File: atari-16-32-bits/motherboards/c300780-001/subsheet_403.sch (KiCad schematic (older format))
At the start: 43 parts, among them Q404 2N3904, Q405 2N3904, U403 MC1377_COLOR_TELEVISION_RGB_T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

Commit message: [PCB] Assign builtins footprint when possible - resistors, ports
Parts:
- D401, D402: footprint (none) -> Diode_THT:D_DO-35_SOD27_P7.62mm_Horizontal
- DL1: footprint (none) -> Delay_Line_Custom_Atari_ST:Delay_Line_Custom_Atari_ST
- MOD1: footprint (none) -> Connector_PinHeader_2.54mm:PinHeader_1x03_P2.54mm_Vertical
- R405, R439, R448, R451, R452, R456, R459, R463, R467, R468, R469, R470, R471, R473, R474, R475: footprint (none) -> Resistor_THT:R_Axial_DIN0204_L3.6mm_D1.6mm_P7.62mm_Horizontal
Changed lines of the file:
@@
 F 0 "R471" V 2300 4650 50  0000 C CNN
 F 1 "47K" V 2500 4650 50  0000 C CNN
-F 2 "" H 2400 4650 50  0001 C CNN
+F 2 "Resistor_THT:R_Axial_DIN0204_L3.6mm_D1.6mm_P7.62mm_Horizontal" H 2400 4650 50  0001 C CNN
 F 3 "~" H 2400 4650 50  0001 C CNN
 	1    2400 4650
@@
 F 0 "R470" H 4680 5920 50  0000 L CNN
 F 1 "1K" H 4680 5860 50  0000 L CNN
-F 2 "" H 4650 5900 50  0001 C CNN
+F 2 "Resistor_THT:R_Axial_DIN0204_L3.6mm_D1.6mm_P7.62mm_Horizontal" H 4650 5900 50  0001 C CNN
 F 3 "~" H 4650 5900 50  0001 C CNN
 	1    4650 5900
@@
 F 0 "R469" V 4300 5650 50  0000 C CNN
 F 1 "5K6" V 4500 5650 50  0000 C CNN
-F 2 "" H 4400 5650 50  0001 C CNN
+F 2 "Resistor_THT:R_Axial_DIN0204_L3.6mm_D1.6mm_P7.62mm_Horizontal" H 4400 5650 50  0001 C CNN
 F 3 "~" H 4400 5650 50  0001 C CNN
 	1    4400 5650
@@
 F 0 "R459" H 7180 5020 50  0000 L CNN
 F 1 "0" H 7180 4960 50  0000 L CNN
-F 2 "" H 7150 5000 50  0001 C CNN
+F 2 "Resistor_THT:R_Axial_DIN0204_L3.6mm_D1.6mm_P7.62mm_Horizontal" H 7150 5000 50  0001 C CNN
 F 3 "~" H 7150 5000 50  0001 C CNN
 	1    7150 5000
@@
 F 0 "R405" V 3850 5950 50  0000 C CNN
 F 1 "0" V 4050 5950 50  0000 C CNN
-F 2 "" H 3950 5950 50  0001 C CNN
+F 2 "Resistor_THT:R_Axial_DIN0204_L3.6mm_D1.6mm_P7.62mm_Horizontal" H 3950 5950 50  0001 C CNN
 F 3 "~" H 3950 5950 50  0001 C CNN
 	1    3950 5950
@@
 F 0 "R439" H 5930 6320 50  0000 L CNN
 F 1 "75" H 5930 6260 50  0000 L CNN
-F 2 "" H 5900 6300 50  0001 C CNN
+F 2 "Resistor_THT:R_Axial_DIN0204_L3.6mm_D1.6mm_P7.62mm_Horizontal" H 5900 6300 50  0001 C CNN
 F 3 "~" H 5900 6300 50  0001 C CNN
 	1    5900 6300
@@
 F 0 "R452" H 5930 7820 50  0000 L CNN
 F 1 "1K5" H 5930 7760 50  0000 L CNN
-F 2 "" H 5900 7800 50  0001 C CNN
+F 2 "Resistor_THT:R_Axial_DIN0204_L3.6mm_D1.6mm_P7.62mm_Horizontal" H 5900 7800 50  0001 C CNN
 F 3 "~" H 5900 7800 50  0001 C CNN
 	1    5900 7800
@@
 F 0 "R456" H 5930 8320 50  0000 L CNN
 F 1 "2K2" H 5930 8260 50  0000 L CNN
-F 2 "" H 5900 8300 50  0001 C CNN
+F 2 "Resistor_THT:R_Axial_DIN0204_L3.6mm_D1.6mm_P7.62mm_Horizontal" H 5900 8300 50  0001 C CNN
 F 3 "~" H 5900 8300 50  0001 C CNN
 	1    5900 8300
@@
 F 0 "DL1" H 2050 6650 50  0000 L CNN
 F 1 "Delay Line 3.58MHz" H 2050 6050 50  0000 L CNN
-F 2 "" H 2000 6350 50  0001 C CNN
+F 2 "Delay_Line_Custom_Atari_ST:Delay_Line_Custom_Atari_ST" H 2000 6350 50  0001 C CNN
 F 3 "~" H 2000 6350 50  0001 C CNN
 	1    2000 6350
@@
 F 0 "R467" H 2030 5770 50  0000 L CNN
 F 1 "1K2" H 2030 5710 50  0000 L CNN
-F 2 "" H 2000 5750 50  0001 C CNN
+F 2 "Resistor_THT:R_Axial_DIN0204_L3.6mm_D1.6mm_P7.62mm_Horizontal" H 2000 5750 50  0001 C CNN
 F 3 "~" H 2000 5750 50  0001 C CNN
 	1    2000 5750
@@
 F 0 "R468" H 2030 7070 50  0000 L CNN
 F 1 "1K2" H 2030 7010 50  0000 L CNN
-F 2 "" H 2000 7050 50  0001 C CNN
+F 2 "Resistor_THT:R_Axial_DIN0204_L3.6mm_D1.6mm_P7.62mm_Horizontal" H 2000 7050 50  0001 C CNN
 F 3 "~" H 2000 7050 50  0001 C CNN
 	1    2000 7050
@@
 F 0 "R448" H 5430 7320 50  0000 L CNN
 F 1 "150" H 5430 7260 50  0000 L CNN
-F 2 "" H 5400 7300 50  0001 C CNN
+F 2 "Resistor_THT:R_Axial_DIN0204_L3.6mm_D1.6mm_P7.62mm_Horizontal" H 5400 7300 50  0001 C CNN
 F 3 "~" H 5400 7300 50  0001 C CNN
 	1    5400 7300
@@
 F 0 "R463" H 3930 8020 50  0000 L CNN
 F 1 "1K" H 3930 7960 50  0000 L CNN
-F 2 "" H 3900 8000 50  0001 C CNN
+F 2 "Resistor_THT:R_Axial_DIN0204_L3.6mm_D1.6mm_P7.62mm_Horizontal" H 3900 8000 50  0001 C CNN
 F 3 "~" H 3900 8000 50  0001 C CNN
 	1    3900 8000
@@
 F 0 "R451" H 4430 7320 50  0000 L CNN
 F 1 "0" H 4430 7260 50  0000 L CNN
-F 2 "" H 4400 7300 50  0001 C CNN
+F 2 "Resistor_THT:R_Axial_DIN0204_L3.6mm_D1.6mm_P7.62mm_Horizontal" H 4400 7300 50  0001 C CNN
 F 3 "~" H 4400 7300 50  0001 C CNN
 	1    4400 7300
@@
 F 0 "MOD1" H 6810 8240 50  0000 C CNN
 F 1 "ST Modulator" H 6840 7860 50  0000 L CNN
-F 2 "" H 6800 8050 50  0001 C CNN
+F 2 "Connector_PinHeader_2.54mm:PinHeader_1x03_P2.54mm_Vertical" H 6800 8050 50  0001 C CNN
 F 3 "~" H 6800 8050 50  0001 C CNN
 	1    6800 8050
@@
 F 0 "R473" H 5830 1320 50  0000 L CNN
 F 1 "10K" H 5830 1260 50  0000 L CNN
-F 2 "" H 5800 1300 50  0001 C CNN
+F 2 "Resistor_THT:R_Axial_DIN0204_L3.6mm_D1.6mm_P7.62mm_Horizontal" H 5800 1300 50  0001 C CNN
 F 3 "~" H 5800 1300 50  0001 C CNN
 	1    5800 1300
@@
 F 0 "R475" H 6280 2170 50  0000 L CNN
 F 1 "150" H 6280 2110 50  0000 L CNN
-F 2 "" H 6250 2150 50  0001 C CNN
+F 2 "Resistor_THT:R_Axial_DIN0204_L3.6mm_D1.6mm_P7.62mm_Horizontal" H 6250 2150 50  0001 C CNN
 F 3 "~" H 6250 2150 50  0001 C CNN
 	1    6250 2150
@@
 F 0 "R474" V 6400 1900 50  0000 C CNN
 F 1 "100" V 6600 1900 50  0000 C CNN
-F 2 "" H 6500 1900 50  0001 C CNN
+F 2 "Resistor_THT:R_Axial_DIN0204_L3.6mm_D1.6mm_P7.62mm_Horizontal" H 6500 1900 50  0001 C CNN
 F 3 "~" H 6500 1900 50  0001 C CNN
 	1    6500 1900
@@
 F 0 "D401" H 5400 1650 50  0000 C CNN
 F 1 "1N914" H 5400 1450 50  0000 C CNN
-F 2 "" H 5400 1550 50  0001 C CNN
+F 2 "Diode_THT:D_DO-35_SOD27_P7.62mm_Horizontal" H 5400 1550 50  0001 C CNN
 F 3 "~" H 5400 1550 50  0001 C CNN
 	1    5400 1550
@@
 F 0 "D402" H 5400 2050 50  0000 C CNN
 F 1 "1N914" H 5400 1850 50  0000 C CNN
-F 2 "" H 5400 1950 50  0001 C CNN
+F 2 "Diode_THT:D_DO-35_SOD27_P7.62mm_Horizontal" H 5400 1950 50  0001 C CNN
 F 3 "~" H 5400 1950 50  0001 C CNN
 	1    5400 1950

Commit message: [PCB] continuing footprint assignement
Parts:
- L403: footprint (none) -> variable_coil_shielded:Variable_Coil_Shielded_7x7mm_5_6
- Q404, Q405: footprint Package_TO_SOT_THT:TO-92_Inline -> Package_TO_SOT_THT:TO-92_Inline_Wide
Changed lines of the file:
@@
 F 0 "Q404" H 5500 6700 50  0000 L CNN
 F 1 "2N3904" H 5450 6600 50  0000 L CNN
-F 2 "Package_TO_SOT_THT:TO-92_Inline" H 5500 6625 50  0001 L CIN
+F 2 "Package_TO_SOT_THT:TO-92_Inline_Wide" H 5500 6625 50  0001 L CIN
 F 3 "https://www.onsemi.com/pub/Collateral/2N3903-D.PDF" H 5300 6700 50  0001 L CNN
 	1    5300 6700
@@
 F 0 "Q405" H 6350 1550 50  0000 L CNN
 F 1 "2N3904" H 6300 1450 50  0000 L CNN
-F 2 "Package_TO_SOT_THT:TO-92_Inline" H 6350 1475 50  0001 L CIN
+F 2 "Package_TO_SOT_THT:TO-92_Inline_Wide" H 6350 1475 50  0001 L CIN
 F 3 "https://www.onsemi.com/pub/Collateral/2N3903-D.PDF" H 6150 1550 50  0001 L CNN
 	1    6150 1550
@@
 F 0 "L403" H 4900 7825 50  0000 C CNN
 F 1 "Variable Coil 24uH" H 4900 7450 50  0000 C CNN
-F 2 "" H 4900 7650 50  0001 C CNN
+F 2 "variable_coil_shielded:Variable_Coil_Shielded_7x7mm_5_6" H 4900 7650 50  0001 C CNN
 F 3 "~" H 4900 7650 50  0001 C CNN
 	1    4900 7650

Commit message: Resolves #41 : [PCB] custom footprint library for passives
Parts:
- D401, D402: footprint Diode_THT:D_DO-35_SOD27_P7.62mm_Horizontal -> commons_passives_THT:Passive_THT_diode_W2.54mm_L12.70mm
- L410: footprint (none) -> commons_passives_THT:Passive_THT_ferrite_bead_W3.81mm_L15.24mm
- R405, R439, R448, R451, R452, R456, R459, R463, R467, R468, R469, R470, R471, R473, R474, R475: footprint Resistor_THT:R_Axial_DIN0204_L3.6mm_D1.6mm_P7.62mm_Horizontal -> commons_passives_THT:Passive_THT_resistor_W2.54mm_L12.70mm
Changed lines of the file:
@@
 F 0 "R471" V 2300 4650 50  0000 C CNN
 F 1 "47K" V 2500 4650 50  0000 C CNN
-F 2 "Resistor_THT:R_Axial_DIN0204_L3.6mm_D1.6mm_P7.62mm_Horizontal" H 2400 4650 50  0001 C CNN
+F 2 "commons_passives_THT:Passive_THT_resistor_W2.54mm_L12.70mm" H 2400 4650 50  0001 C CNN
 F 3 "~" H 2400 4650 50  0001 C CNN
 	1    2400 4650
@@
 F 0 "R470" H 4680 5920 50  0000 L CNN
 F 1 "1K" H 4680 5860 50  0000 L CNN
-F 2 "Resistor_THT:R_Axial_DIN0204_L3.6mm_D1.6mm_P7.62mm_Horizontal" H 4650 5900 50  0001 C CNN
+F 2 "commons_passives_THT:Passive_THT_resistor_W2.54mm_L12.70mm" H 4650 5900 50  0001 C CNN
 F 3 "~" H 4650 5900 50  0001 C CNN
 	1    4650 5900
@@
 F 0 "R469" V 4300 5650 50  0000 C CNN
 F 1 "5K6" V 4500 5650 50  0000 C CNN
-F 2 "Resistor_THT:R_Axial_DIN0204_L3.6mm_D1.6mm_P7.62mm_Horizontal" H 4400 5650 50  0001 C CNN
+F 2 "commons_passives_THT:Passive_THT_resistor_W2.54mm_L12.70mm" H 4400 5650 50  0001 C CNN
 F 3 "~" H 4400 5650 50  0001 C CNN
 	1    4400 5650
@@
 F 0 "R459" H 7180 5020 50  0000 L CNN
 F 1 "0" H 7180 4960 50  0000 L CNN
-F 2 "Resistor_THT:R_Axial_DIN0204_L3.6mm_D1.6mm_P7.62mm_Horizontal" H 7150 5000 50  0001 C CNN
+F 2 "commons_passives_THT:Passive_THT_resistor_W2.54mm_L12.70mm" H 7150 5000 50  0001 C CNN
 F 3 "~" H 7150 5000 50  0001 C CNN
 	1    7150 5000
@@
 F 0 "R405" V 3850 5950 50  0000 C CNN
 F 1 "0" V 4050 5950 50  0000 C CNN
-F 2 "Resistor_THT:R_Axial_DIN0204_L3.6mm_D1.6mm_P7.62mm_Horizontal" H 3950 5950 50  0001 C CNN
+F 2 "commons_passives_THT:Passive_THT_resistor_W2.54mm_L12.70mm" H 3950 5950 50  0001 C CNN
 F 3 "~" H 3950 5950 50  0001 C CNN
 	1    3950 5950
@@
 F 0 "R439" H 5930 6320 50  0000 L CNN
 F 1 "75" H 5930 6260 50  0000 L CNN
-F 2 "Resistor_THT:R_Axial_DIN0204_L3.6mm_D1.6mm_P7.62mm_Horizontal" H 5900 6300 50  0001 C CNN
+F 2 "commons_passives_THT:Passive_THT_resistor_W2.54mm_L12.70mm" H 5900 6300 50  0001 C CNN
 F 3 "~" H 5900 6300 50  0001 C CNN
 	1    5900 6300
@@
 F 0 "R452" H 5930 7820 50  0000 L CNN
 F 1 "1K5" H 5930 7760 50  0000 L CNN
-F 2 "Resistor_THT:R_Axial_DIN0204_L3.6mm_D1.6mm_P7.62mm_Horizontal" H 5900 7800 50  0001 C CNN
+F 2 "commons_passives_THT:Passive_THT_resistor_W2.54mm_L12.70mm" H 5900 7800 50  0001 C CNN
 F 3 "~" H 5900 7800 50  0001 C CNN
 	1    5900 7800
@@
 F 0 "R456" H 5930 8320 50  0000 L CNN
 F 1 "2K2" H 5930 8260 50  0000 L CNN
-F 2 "Resistor_THT:R_Axial_DIN0204_L3.6mm_D1.6mm_P7.62mm_Horizontal" H 5900 8300 50  0001 C CNN
+F 2 "commons_passives_THT:Passive_THT_resistor_W2.54mm_L12.70mm" H 5900 8300 50  0001 C CNN
 F 3 "~" H 5900 8300 50  0001 C CNN
 	1    5900 8300
@@
 F 0 "R467" H 2030 5770 50  0000 L CNN
 F 1 "1K2" H 2030 5710 50  0000 L CNN
-F 2 "Resistor_THT:R_Axial_DIN0204_L3.6mm_D1.6mm_P7.62mm_Horizontal" H 2000 5750 50  0001 C CNN
+F 2 "commons_passives_THT:Passive_THT_resistor_W2.54mm_L12.70mm" H 2000 5750 50  0001 C CNN
 F 3 "~" H 2000 5750 50  0001 C CNN
 	1    2000 5750
@@
 F 0 "R468" H 2030 7070 50  0000 L CNN
 F 1 "1K2" H 2030 7010 50  0000 L CNN
-F 2 "Resistor_THT:R_Axial_DIN0204_L3.6mm_D1.6mm_P7.62mm_Horizontal" H 2000 7050 50  0001 C CNN
+F 2 "commons_passives_THT:Passive_THT_resistor_W2.54mm_L12.70mm" H 2000 7050 50  0001 C CNN
 F 3 "~" H 2000 7050 50  0001 C CNN
 	1    2000 7050
@@
 F 0 "L410" H 1575 1550 50  0000 L CNN
 F 1 "Ferrite Bead" H 1575 1450 50  0000 L CNN
-F 2 "" V 1430 1500 50  0001 C CNN
+F 2 "commons_passives_THT:Passive_THT_ferrite_bead_W3.81mm_L15.24mm" V 1430 1500 50  0001 C CNN
 F 3 "~" H 1500 1500 50  0001 C CNN
 	1    1500 1500
@@
 F 0 "R448" H 5430 7320 50  0000 L CNN
 F 1 "150" H 5430 7260 50  0000 L CNN
-F 2 "Resistor_THT:R_Axial_DIN0204_L3.6mm_D1.6mm_P7.62mm_Horizontal" H 5400 7300 50  0001 C CNN
+F 2 "commons_passives_THT:Passive_THT_resistor_W2.54mm_L12.70mm" H 5400 7300 50  0001 C CNN
 F 3 "~" H 5400 7300 50  0001 C CNN
 	1    5400 7300
@@
 F 0 "R463" H 3930 8020 50  0000 L CNN
 F 1 "1K" H 3930 7960 50  0000 L CNN
-F 2 "Resistor_THT:R_Axial_DIN0204_L3.6mm_D1.6mm_P7.62mm_Horizontal" H 3900 8000 50  0001 C CNN
+F 2 "commons_passives_THT:Passive_THT_resistor_W2.54mm_L12.70mm" H 3900 8000 50  0001 C CNN
 F 3 "~" H 3900 8000 50  0001 C CNN
 	1    3900 8000
@@
 F 0 "R451" H 4430 7320 50  0000 L CNN
 F 1 "0" H 4430 7260 50  0000 L CNN
-F 2 "Resistor_THT:R_Axial_DIN0204_L3.6mm_D1.6mm_P7.62mm_Horizontal" H 4400 7300 50  0001 C CNN
+F 2 "commons_passives_THT:Passive_THT_resistor_W2.54mm_L12.70mm" H 4400 7300 50  0001 C CNN
 F 3 "~" H 4400 7300 50  0001 C CNN
 	1    4400 7300
@@
 F 0 "R473" H 5830 1320 50  0000 L CNN
 F 1 "10K" H 5830 1260 50  0000 L CNN
-F 2 "Resistor_THT:R_Axial_DIN0204_L3.6mm_D1.6mm_P7.62mm_Horizontal" H 5800 1300 50  0001 C CNN
+F 2 "commons_passives_THT:Passive_THT_resistor_W2.54mm_L12.70mm" H 5800 1300 50  0001 C CNN
 F 3 "~" H 5800 1300 50  0001 C CNN
 	1    5800 1300
@@
 F 0 "R475" H 6280 2170 50  0000 L CNN
 F 1 "150" H 6280 2110 50  0000 L CNN
-F 2 "Resistor_THT:R_Axial_DIN0204_L3.6mm_D1.6mm_P7.62mm_Horizontal" H 6250 2150 50  0001 C CNN
+F 2 "commons_passives_THT:Passive_THT_resistor_W2.54mm_L12.70mm" H 6250 2150 50  0001 C CNN
 F 3 "~" H 6250 2150 50  0001 C CNN
 	1    6250 2150
@@
 F 0 "R474" V 6400 1900 50  0000 C CNN
 F 1 "100" V 6600 1900 50  0000 C CNN
-F 2 "Resistor_THT:R_Axial_DIN0204_L3.6mm_D1.6mm_P7.62mm_Horizontal" H 6500 1900 50  0001 C CNN
+F 2 "commons_passives_THT:Passive_THT_resistor_W2.54mm_L12.70mm" H 6500 1900 50  0001 C CNN
 F 3 "~" H 6500 1900 50  0001 C CNN
 	1    6500 1900
@@
 F 0 "D401" H 5400 1650 50  0000 C CNN
 F 1 "1N914" H 5400 1450 50  0000 C CNN
-F 2 "Diode_THT:D_DO-35_SOD27_P7.62mm_Horizontal" H 5400 1550 50  0001 C CNN
+F 2 "commons_passives_THT:Passive_THT_diode_W2.54mm_L12.70mm" H 5400 1550 50  0001 C CNN
 F 3 "~" H 5400 1550 50  0001 C CNN
 	1    5400 1550
@@
 F 0 "D402" H 5400 2050 50  0000 C CNN
 F 1 "1N914" H 5400 1850 50  0000 C CNN
-F 2 "Diode_THT:D_DO-35_SOD27_P7.62mm_Horizontal" H 5400 1950 50  0001 C CNN
+F 2 "commons_passives_THT:Passive_THT_diode_W2.54mm_L12.70mm" H 5400 1950 50  0001 C CNN
 F 3 "~" H 5400 1950 50  0001 C CNN
 	1    5400 1950

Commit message: [PCB] continue footprint assignation
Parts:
- C419, C422, C428, C429: footprint (none) -> commons_passives_THT:Passive_THT_capacitor_ceramic_radial_W5.08mm_L6.35mm_X11.43mm
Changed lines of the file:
@@
 F 0 "C419" H 5825 3750 50  0000 L CNN
 F 1 "0.1uF" H 5825 3550 50  0000 L CNN
-F 2 "" H 5838 3500 50  0001 C CNN
+F 2 "commons_passives_THT:Passive_THT_capacitor_ceramic_radial_W5.08mm_L6.35mm_X11.43mm" H 5838 3500 50  0001 C CNN
 F 3 "~" H 5800 3650 50  0001 C CNN
 	1    5800 3650
@@
 F 0 "C428" H 5175 5100 50  0000 L CNN
 F 1 "0.1uF" H 5175 4900 50  0000 L CNN
-F 2 "" H 5188 4850 50  0001 C CNN
+F 2 "commons_passives_THT:Passive_THT_capacitor_ceramic_radial_W5.08mm_L6.35mm_X11.43mm" H 5188 4850 50  0001 C CNN
 F 3 "~" H 5150 5000 50  0001 C CNN
 	1    5150 5000
@@
 F 0 "C429" H 5675 5100 50  0000 L CNN
 F 1 "0.1uF" H 5675 4900 50  0000 L CNN
-F 2 "" H 5688 4850 50  0001 C CNN
+F 2 "commons_passives_THT:Passive_THT_capacitor_ceramic_radial_W5.08mm_L6.35mm_X11.43mm" H 5688 4850 50  0001 C CNN
 F 3 "~" H 5650 5000 50  0001 C CNN
 	1    5650 5000
@@
 F 0 "C422" H 1175 5100 50  0000 L CNN
 F 1 "0.1uF" H 1175 4900 50  0000 L CNN
-F 2 "" H 1188 4850 50  0001 C CNN
+F 2 "commons_passives_THT:Passive_THT_capacitor_ceramic_radial_W5.08mm_L6.35mm_X11.43mm" H 1188 4850 50  0001 C CNN
 F 3 "~" H 1150 5000 50  0001 C CNN
 	1    1150 5000

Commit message: [PCB] continue footprints assignements
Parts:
- C420, C424, C426: footprint (none) -> Capacitor_THT:CP_Radial_Tantal_D4.5mm_P2.50mm
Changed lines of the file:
@@
 F 0 "C420" H 3175 5100 50  0000 L CNN
 F 1 "15uF" H 3175 4900 50  0000 L CNN
-F 2 "" H 3150 5000 50  0001 C CNN
+F 2 "Capacitor_THT:CP_Radial_Tantal_D4.5mm_P2.50mm" H 3150 5000 50  0001 C CNN
 F 3 "~" H 3150 5000 50  0001 C CNN
 	1    3150 5000
@@
 F 0 "C424" H 3675 5100 50  0000 L CNN
 F 1 "15uF" H 3675 4900 50  0000 L CNN
-F 2 "" H 3650 5000 50  0001 C CNN
+F 2 "Capacitor_THT:CP_Radial_Tantal_D4.5mm_P2.50mm" H 3650 5000 50  0001 C CNN
 F 3 "~" H 3650 5000 50  0001 C CNN
 	1    3650 5000
@@
 F 0 "C426" H 4175 5100 50  0000 L CNN
 F 1 "15uF" H 4175 4900 50  0000 L CNN
-F 2 "" H 4150 5000 50  0001 C CNN
+F 2 "Capacitor_THT:CP_Radial_Tantal_D4.5mm_P2.50mm" H 4150 5000 50  0001 C CNN
 F 3 "~" H 4150 5000 50  0001 C CNN
 	1    4150 5000

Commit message: [PCB] continue assigning footprints - done all fixed capacitors
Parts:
- C415: footprint (none) -> commons_passives_THT:Passive_THT_capacitor_polarized_rad_D10.16mm_P5.08mm_H22.86mm
- C417, C423, C425, C433: footprint (none) -> commons_passives_THT:Passive_THT_capacitor_polarized_rad_D5.08mm_P2.54mm_H12.70mm
- C418, C421, C427, C430, C431: footprint (none) -> commons_passives_THT:Passive_THT_capacitor_W2.54mm_L10.16mm
- C432: footprint (none) -> commons_passives_THT:Passive_THT_capacitor_ceramic_radial_W2.54mm_L10.16mm
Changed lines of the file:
@@
 F 0 "C430" H 6175 5100 50  0000 L CNN
 F 1 "0.01uF" H 6175 4900 50  0000 L CNN
-F 2 "" H 6188 4850 50  0001 C CNN
+F 2 "commons_passives_THT:Passive_THT_capacitor_W2.54mm_L10.16mm" H 6188 4850 50  0001 C CNN
 F 3 "~" H 6150 5000 50  0001 C CNN
 	1    6150 5000
@@
 F 0 "C431" H 6675 5100 50  0000 L CNN
 F 1 "0.01uF" H 6675 4900 50  0000 L CNN
-F 2 "" H 6688 4850 50  0001 C CNN
+F 2 "commons_passives_THT:Passive_THT_capacitor_W2.54mm_L10.16mm" H 6688 4850 50  0001 C CNN
 F 3 "~" H 6650 5000 50  0001 C CNN
 	1    6650 5000
@@
 F 0 "C432" H 2175 5100 50  0000 L CNN
 F 1 "0.001uF" H 2175 4900 50  0000 L CNN
-F 2 "" H 2188 4850 50  0001 C CNN
+F 2 "commons_passives_THT:Passive_THT_capacitor_ceramic_radial_W2.54mm_L10.16mm" H 2188 4850 50  0001 C CNN
 F 3 "~" H 2150 5000 50  0001 C CNN
 	1    2150 5000
@@
 F 0 "C433" H 2675 5100 50  0000 L CNN
 F 1 "1uF" H 2675 4900 50  0000 L CNN
-F 2 "" H 2650 5000 50  0001 C CNN
+F 2 "commons_passives_THT:Passive_THT_capacitor_polarized_rad_D5.08mm_P2.54mm_H12.70mm" H 2650 5000 50  0001 C CNN
 F 3 "~" H 2650 5000 50  0001 C CNN
 	1    2650 5000
@@
 F 0 "C427" H 4675 5100 50  0000 L CNN
 F 1 "0.001uF" H 4675 4900 50  0000 L CNN
-F 2 "" H 4688 4850 50  0001 C CNN
+F 2 "commons_passives_THT:Passive_THT_capacitor_W2.54mm_L10.16mm" H 4688 4850 50  0001 C CNN
 F 3 "~" H 4650 5000 50  0001 C CNN
 	1    4650 5000
@@
 F 0 "C415" H 5925 6850 50  0000 L CNN
 F 1 "470uF" H 5925 6650 50  0000 L CNN
-F 2 "" H 5900 6750 50  0001 C CNN
+F 2 "commons_passives_THT:Passive_THT_capacitor_polarized_rad_D10.16mm_P5.08mm_H22.86mm" H 5900 6750 50  0001 C CNN
 F 3 "~" H 5900 6750 50  0001 C CNN
 	1    5900 6750
@@
 F 0 "C417" H 5925 7450 50  0000 L CNN
 F 1 "100uF" H 5925 7250 50  0000 L CNN
-F 2 "" H 5900 7350 50  0001 C CNN
+F 2 "commons_passives_THT:Passive_THT_capacitor_polarized_rad_D5.08mm_P2.54mm_H12.70mm" H 5900 7350 50  0001 C CNN
 F 3 "~" H 5900 7350 50  0001 C CNN
 	1    5900 7350
@@
 F 0 "C421" H 4425 8150 50  0000 L CNN
 F 1 "120pF" H 4425 7950 50  0000 L CNN
-F 2 "" H 4438 7900 50  0001 C CNN
+F 2 "commons_passives_THT:Passive_THT_capacitor_W2.54mm_L10.16mm" H 4438 7900 50  0001 C CNN
 F 3 "~" H 4400 8050 50  0001 C CNN
 	1    4400 8050
@@
 F 0 "C425" H 3925 7550 50  0000 L CNN
 F 1 "2200pF" H 3925 7350 50  0000 L CNN
-F 2 "" H 3938 7300 50  0001 C CNN
+F 2 "commons_passives_THT:Passive_THT_capacitor_polarized_rad_D5.08mm_P2.54mm_H12.70mm" H 3938 7300 50  0001 C CNN
 F 3 "~" H 3900 7450 50  0001 C CNN
 	1    3900 7450
@@
 F 0 "C418" H 4425 6950 50  0000 L CNN
 F 1 "2200pF" H 4425 6750 50  0000 L CNN
-F 2 "" H 4438 6700 50  0001 C CNN
+F 2 "commons_passives_THT:Passive_THT_capacitor_W2.54mm_L10.16mm" H 4438 6700 50  0001 C CNN
 F 3 "~" H 4400 6850 50  0001 C CNN
 	1    4400 6850
@@
 F 0 "C423" H 1675 5100 50  0000 L CNN
 F 1 "100uF" H 1675 4900 50  0000 L CNN
-F 2 "" H 1650 5000 50  0001 C CNN
+F 2 "commons_passives_THT:Passive_THT_capacitor_polarized_rad_D5.08mm_P2.54mm_H12.70mm" H 1650 5000 50  0001 C CNN
 F 3 "~" H 1650 5000 50  0001 C CNN
 	1    1650 5000

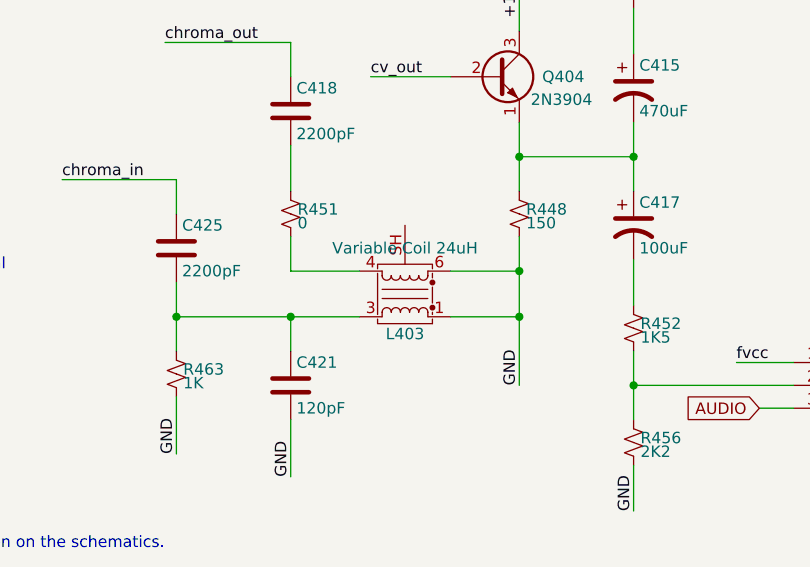
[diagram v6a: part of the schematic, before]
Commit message: Resolves #47 : [Schematics][PCB] Variable coil - the symbol should have a shield pin, its Footprint should name 'SH' the pins for the shields
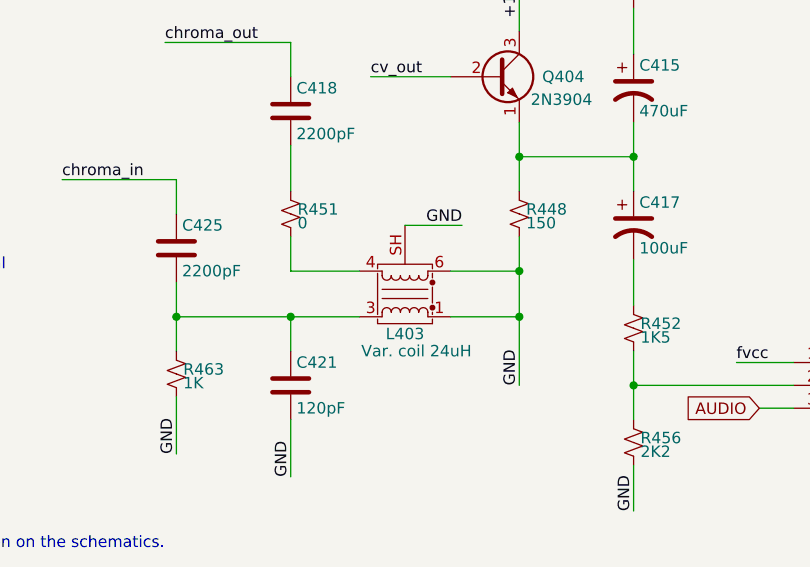
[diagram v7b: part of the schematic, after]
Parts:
- L403: value Variable Coil 24uH -> Var. coil 24uH
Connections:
- net GND: now also L403.SH (Shield)
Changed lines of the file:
@@
 P 4900 7650
 F 0 "L403" H 4900 7825 50  0000 C CNN
-F 1 "Variable Coil 24uH" H 4900 7450 50  0000 C CNN
+F 1 "Var. coil 24uH" H 4850 7900 50  0000 C CNN
 F 2 "variable_coil_shielded:Variable_Coil_Shielded_7x7mm_5_6" H 4900 7650 50  0001 C CNN
 F 3 "~" H 4900 7650 50  0001 C CNN
@@
 	2150 6550 2550 6550
 Connection ~ 4650 5650
+Wire Wire Line
+	4900 7350 5150 7350
+Text Label 5150 7350 2    50   ~ 0
+GND
 $EndSCHEMATC

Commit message: migrate to kicad-footprints-handmade
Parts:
- DL1: footprint Delay_Line_Custom_Atari_ST:Delay_Line_Custom_Atari_ST -> atari-passives_THT:Atari_ST_THT_Delay_Line
- L403: footprint variable_coil_shielded:Variable_Coil_Shielded_7x7mm_5_6 -> commons_passives_THT:Passive_THT_variable_Coil_Shielded_7x7mm_5_of_6pins
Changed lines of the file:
@@
 F 0 "DL1" H 2050 6650 50  0000 L CNN
 F 1 "Delay Line 3.58MHz" H 2050 6050 50  0000 L CNN
-F 2 "Delay_Line_Custom_Atari_ST:Delay_Line_Custom_Atari_ST" H 2000 6350 50  0001 C CNN
+F 2 "atari-passives_THT:Atari_ST_THT_Delay_Line" H 2000 6350 50  0001 C CNN
 F 3 "~" H 2000 6350 50  0001 C CNN
 	1    2000 6350
@@
 F 0 "L403" H 4900 7825 50  0000 C CNN
 F 1 "Var. coil 24uH" H 4850 7900 50  0000 C CNN
-F 2 "variable_coil_shielded:Variable_Coil_Shielded_7x7mm_5_6" H 4900 7650 50  0001 C CNN
+F 2 "commons_passives_THT:Passive_THT_variable_Coil_Shielded_7x7mm_5_of_6pins" H 4900 7650 50  0001 C CNN
 F 3 "~" H 4900 7650 50  0001 C CNN
 	1    4900 7650
